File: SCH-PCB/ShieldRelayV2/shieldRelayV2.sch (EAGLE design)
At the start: 89 parts, among them IC1 LM2596SX-5.0_NOPB, IC2 LM1117MPX-33NOPB, IC3 FT231XS-R, K1 SLA-05VDC-SL-C, K2 SRD-05VDC-SL-C, K3 G3MB-202PL-DC5, K5 G3MB-202PL-DC5, K6 SRD-05VDC-SL-C, Q1 MMST2222A-7-F, Q2 MMST2222A-7-F, Q3 MMST2222A-7-F, Q4 MMST2222A-7-F, Q5 MMST2222A-7-F, Q6 MMBT3904-TP, Q7 MMBT3904-TP

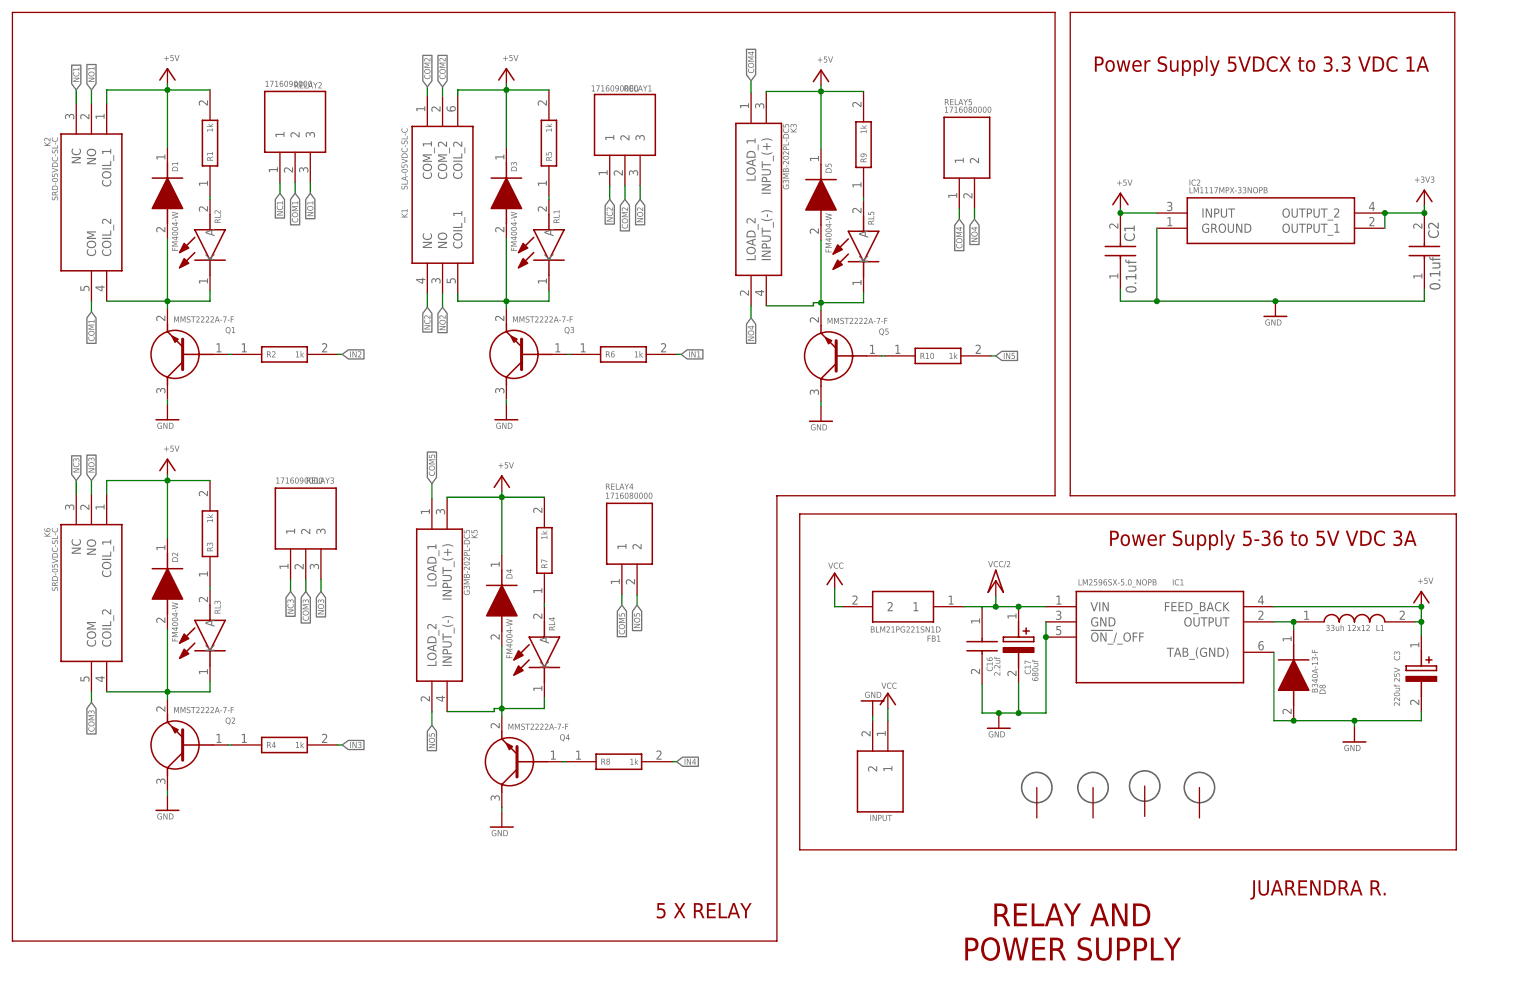
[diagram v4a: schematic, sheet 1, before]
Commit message: FIX: fix reverse transistor relay
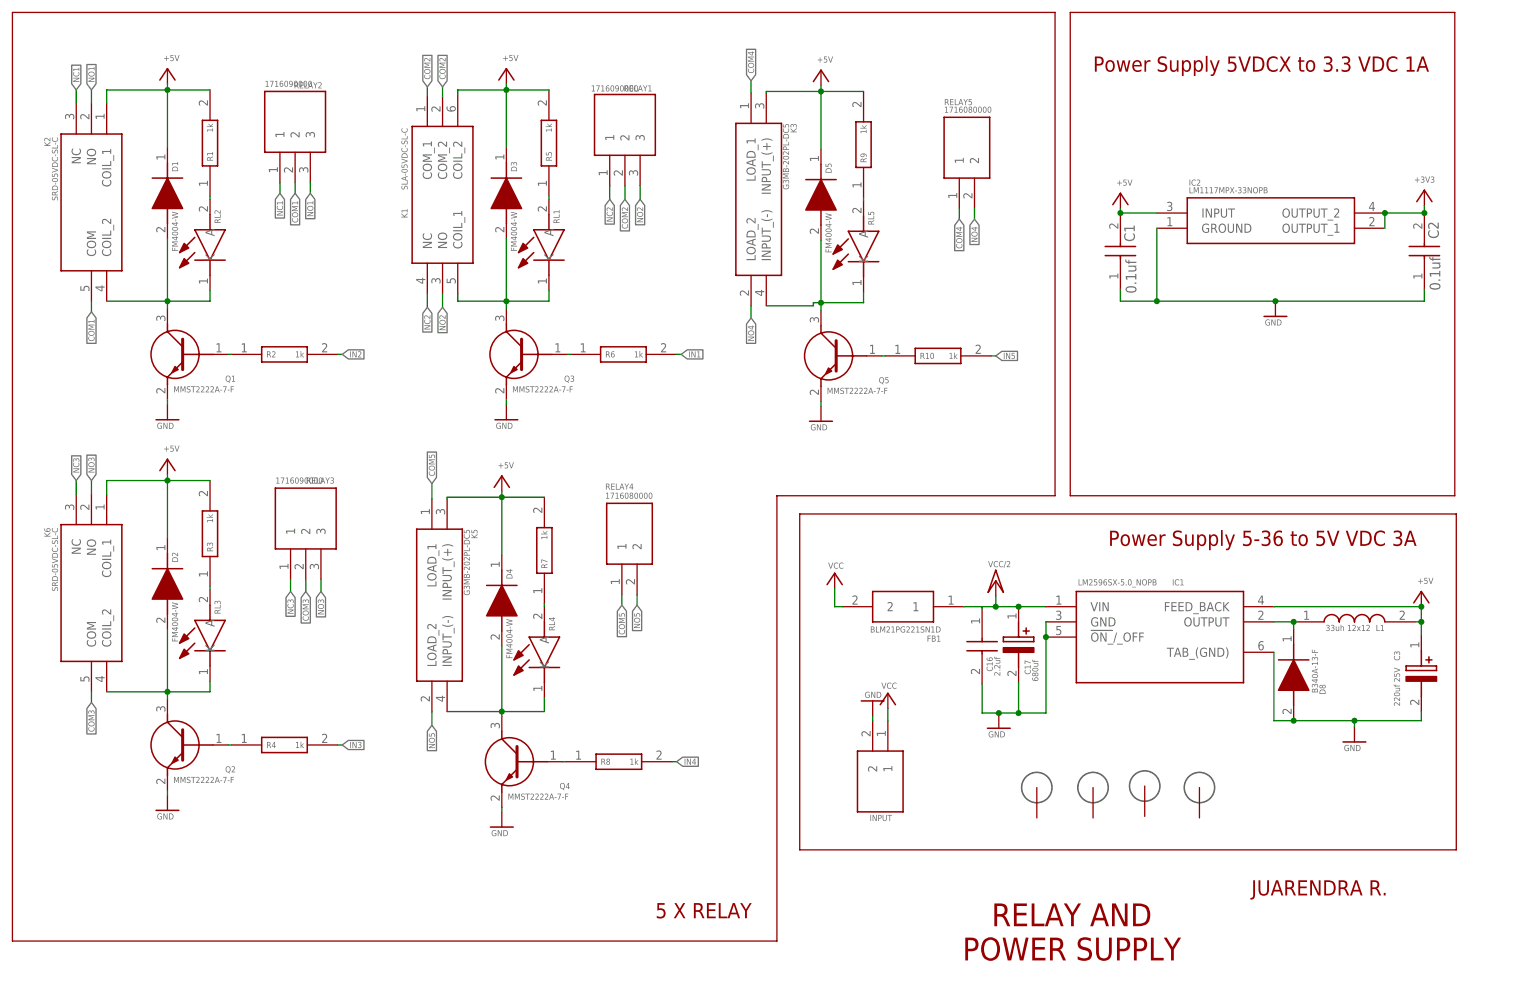
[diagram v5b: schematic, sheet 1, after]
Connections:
- net GND: now also Q1.E, Q2.E, Q3.E, Q4.E, Q5.E; no longer Q1.C, Q2.C, Q3.C, Q4.C, Q5.C
- net N$11: now also Q4.C; no longer Q4.E
- net N$14: now also Q5.C; no longer Q5.E
- net N$3: now also Q1.C; no longer Q1.E
- net N$5: now also Q2.C; no longer Q2.E
- net N$8: now also Q3.C; no longer Q3.E
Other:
- moved on the sheet: Q1, Q2, Q3, Q4, Q5
